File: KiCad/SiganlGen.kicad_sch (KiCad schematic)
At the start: 79 parts, among them J1 Barrel_Jack_MountingPin, J2 Conn_Coaxial, J3 Conn_01x08_Socket, Q1 BC557, Q2 BC547, SW1 RotaryEncoder_Switch, SW10 SW_Push_45deg, SW11 SW_Push_45deg, SW12 SW_Push_45deg, SW13 SW_Push_45deg, SW14 SW_Push_45deg, SW15 SW_Push_45deg, SW16 SW_Push_45deg, SW17 SW_Push_45deg, SW18 SW_Push, SW19 SW_Push, SW2 SW_Push_45deg, SW20 SW_Push, SW21 SW_Push, SW3 SW_Push_45deg, SW4 SW_Push_45deg, SW5 SW_Push_45deg, SW6 SW_Push_45deg, SW7 SW_Push_45deg, SW8 SW_Push_45deg, SW9 SW_Push_45deg, U1 RaspberryPi_Pico, U3 NE5532, U4 MC34063AP, U5 NE5532, U6 LM7910_TO220, U7 LM7810_TO220, U8 LM7805_TO220

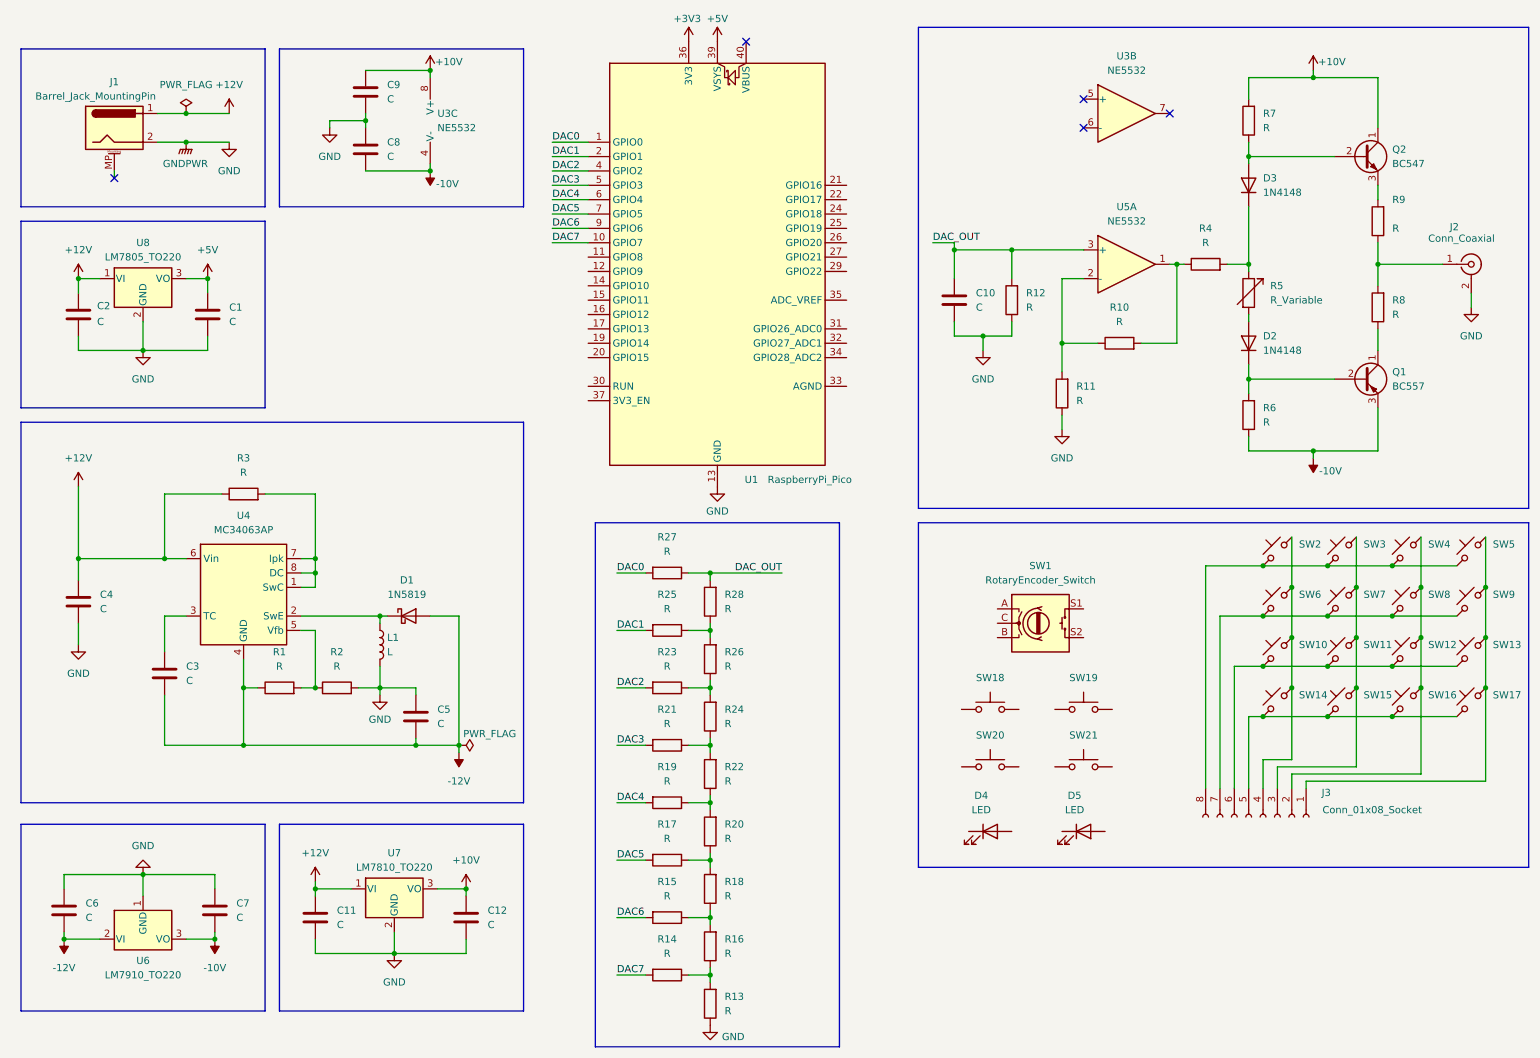
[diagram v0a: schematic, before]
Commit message: Partition schematic to different sheets
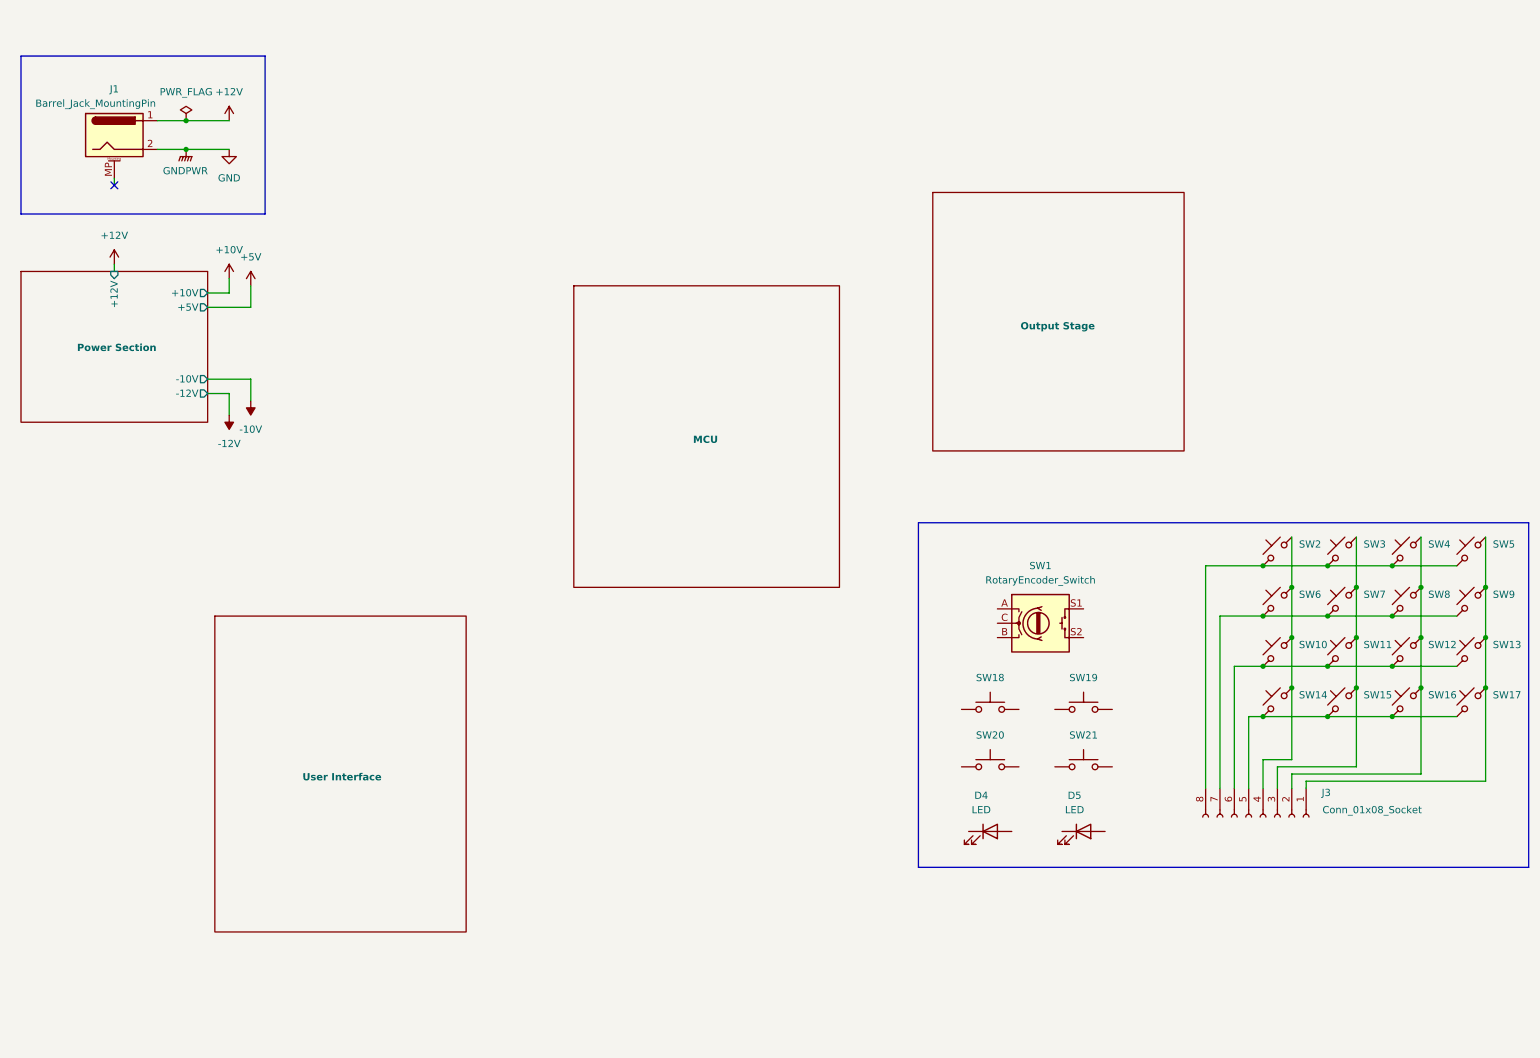
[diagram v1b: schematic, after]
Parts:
- removed C1, C10, C11, C12, C2, C3, C4, C5, C6, C7, C8, C9: C, symbol Device:C
- removed D1: 1N5819, Diode_THT:D_DO-41_SOD81_P10.16mm_Horizontal, symbol Diode:1N5819
- removed D2, D3: 1N4148, Diode_THT:D_DO-35_SOD27_P7.62mm_Horizontal, symbol Diode:1N4148
- removed J2: Conn_Coaxial, symbol Connector:Conn_Coaxial
- removed L1: L, symbol Device:L
- removed Q1: BC557, Package_TO_SOT_THT:TO-92_HandSolder, symbol Transistor_BJT:BC557
- removed Q2: BC547, Package_TO_SOT_THT:TO-92_HandSolder, symbol Transistor_BJT:BC547
- removed R1, R10, R11, R12, R13, R14, R15, R16, R17, R18, R19, R2, R20, R21, R22, R23, R24, R25, R26, R27, R28, R3, R4, R6, R7, R8, R9: R, symbol Device:R
- removed R5: R_Variable, symbol Device:R_Variable
- removed U1: RaspberryPi_Pico, Module_RaspberryPi_Pico:RaspberryPi_Pico_Common, symbol MCU_Module_RaspberryPi_Pico:RaspberryPi_Pico
- removed U3, U5: NE5532, Package_DIP:DIP-8_W7.62mm_Socket_LongPads, symbol Amplifier_Operational:NE5532
- removed U4: MC34063AP, Package_DIP:DIP-8_W7.62mm_Socket_LongPads, symbol Regulator_Switching:MC34063AP
- removed U6: LM7910_TO220, Package_TO_SOT_THT:TO-220-3_Vertical, symbol Regulator_Linear:LM7910_TO220
- removed U7: LM7810_TO220, Package_TO_SOT_THT:TO-220-3_Vertical, symbol Regulator_Linear:LM7810_TO220
- removed U8: LM7805_TO220, Package_TO_SOT_THT:TO-220-3_Vertical, symbol Regulator_Linear:LM7805_TO220
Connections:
- no-connect marks 5 -> 1
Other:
- added sheet MCU (MCU.kicad_sch)
- added sheet Output Stage (OutputStage.kicad_sch)
- added sheet Power Section (PowerSection.kicad_sch)
- added sheet User Interface (UserInterface.kicad_sch)
- moved on the sheet: J1

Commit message: Filled in schematic
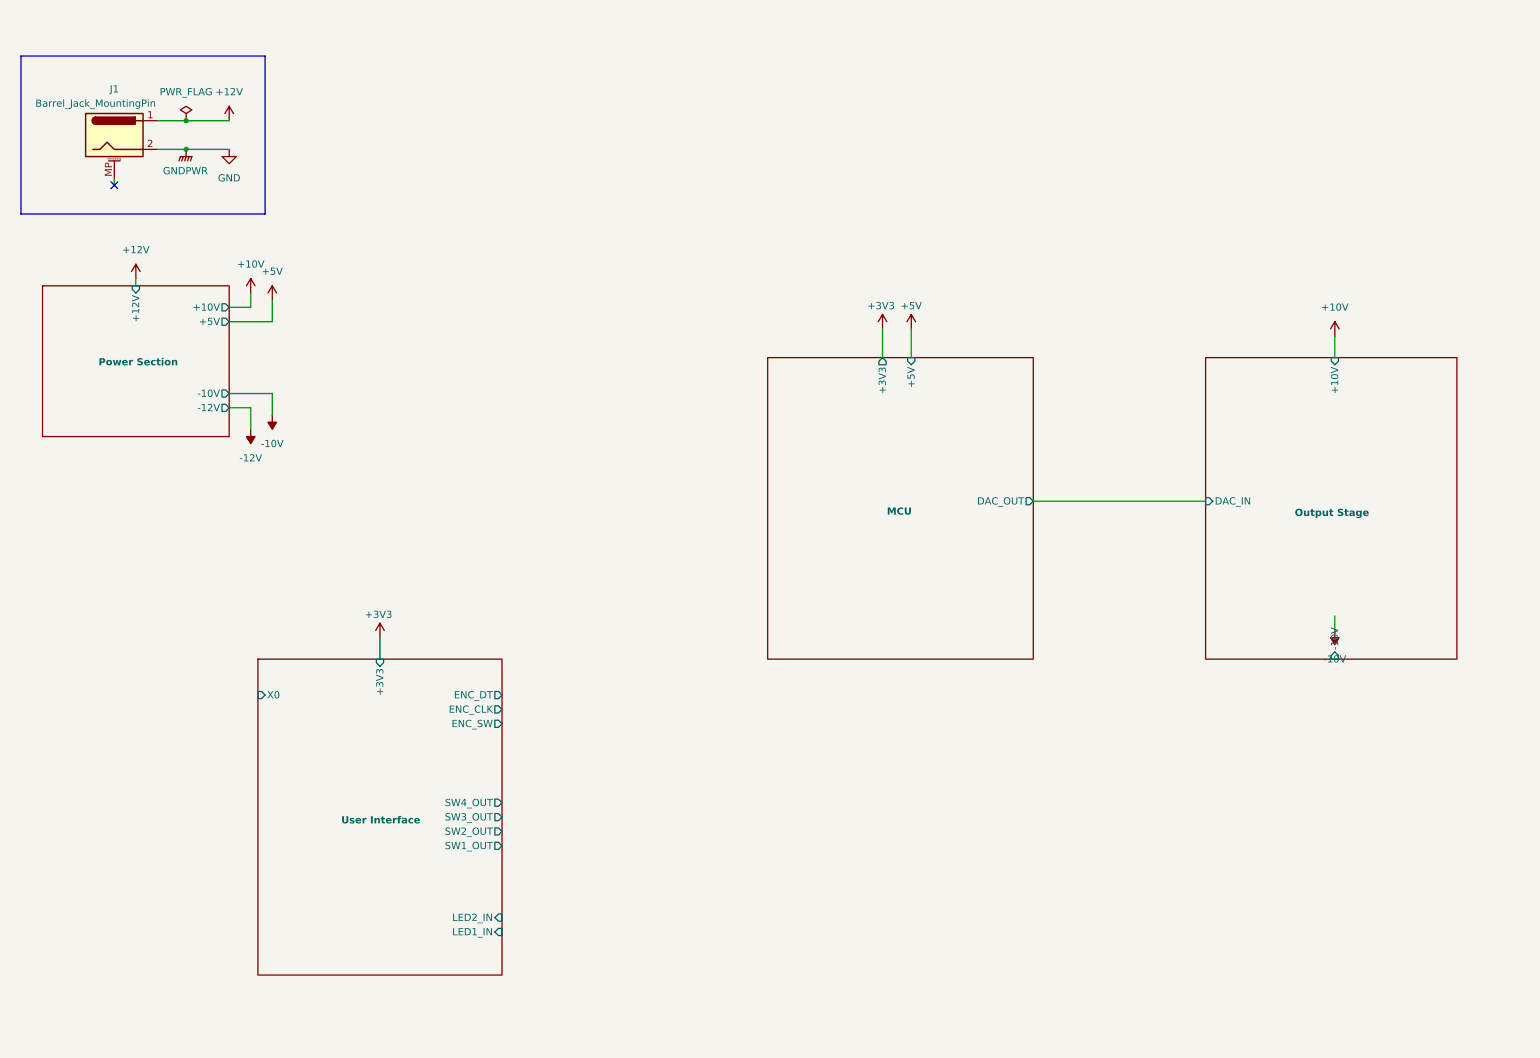
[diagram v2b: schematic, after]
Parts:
- removed D4, D5: LED, symbol Device:LED
- removed J3: Conn_01x08_Socket, symbol Connector:Conn_01x08_Socket
- removed SW1: RotaryEncoder_Switch, symbol Device:RotaryEncoder_Switch
- removed SW10, SW11, SW12, SW13, SW14, SW15, SW16, SW17, SW2, SW3, SW4, SW5, SW6, SW7, SW8, SW9: SW_Push_45deg, symbol Switch:SW_Push_45deg
- removed SW18, SW19, SW20, SW21: SW_Push, symbol Switch:SW_Push
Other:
- sheet MCU ports: added +3V3, +5V, DAC_OUT; removed none
- sheet Output Stage ports: added +10V, -10V, DAC_IN; removed none
- sheet User Interface ports: added +3V3, ENC_CLK, ENC_DT, ENC_SW, LED1_IN, LED2_IN, SW1_OUT, SW2_OUT, SW3_OUT, SW4_OUT, X0; removed none

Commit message: minor changes
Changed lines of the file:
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@@
 	(wire
 		(pts
-			(xy 195.58 99.06) (xy 226.06 99.06)
+			(xy 179.07 85.09) (xy 209.55 85.09)
 		)
 		(stroke
@@
 	(wire
 		(pts
-			(xy 173.99 68.58) (xy 173.99 73.66)
+			(xy 157.48 54.61) (xy 157.48 59.69)
 		)
 		(stroke
@@
 	(wire
 		(pts
-			(xy 248.92 119.38) (xy 248.92 121.92)
-		)
-		(stroke
-			(width 0)
-			(type default)
-		)
-	)
-	(wire
-		(pts
-			(xy 168.91 68.58) (xy 168.91 73.66)
+			(xy 232.41 105.41) (xy 232.41 107.95)
+		)
+		(stroke
+			(width 0)
+			(type default)
+		)
+	)
+	(wire
+		(pts
+			(xy 152.4 54.61) (xy 152.4 59.69)
 		)
 		(stroke
@@
 	(wire
 		(pts
-			(xy 248.92 69.85) (xy 248.92 73.66)
+			(xy 232.41 55.88) (xy 232.41 59.69)
 		)
 		(stroke
@@
 	(symbol
 		(lib_id "power:+3V3")
-		(at 168.91 68.58 0)
+		(at 152.4 54.61 0)
 		(unit 1)
 		(exclude_from_sim no)
@@
 		(dnp no)
 		(property "Reference" "#PWR011"
-			(at 168.91 72.39 0)
+			(at 152.4 58.42 0)
 			(effects
 				(font
@@
 		)
 		(property "Value" "+3V3"
-			(at 168.656 64.516 0)
+			(at 152.146 50.546 0)
 			(effects
 				(font
@@
 		)
 		(property "Footprint" ""
-			(at 168.91 68.58 0)
+			(at 152.4 54.61 0)
 			(effects
 				(font
@@
 		)
 		(property "Datasheet" ""
-			(at 168.91 68.58 0)
+			(at 152.4 54.61 0)
 			(effects
 				(font
@@
 		)
 		(property "Description" "Power symbol creates a global label with name \"+3V3\""
-			(at 168.91 68.58 0)
+			(at 152.4 54.61 0)
 			(effects
 				(font
@@
 	(symbol
 		(lib_id "power:+5V")
-		(at 173.99 68.58 0)
+		(at 157.48 54.61 0)
 		(unit 1)
 		(exclude_from_sim no)
@@
 		(dnp no)
 		(property "Reference" "#PWR016"
-			(at 173.99 72.39 0)
+			(at 157.48 58.42 0)
 			(effects
 				(font
@@
 		)
 		(property "Value" "+5V"
-			(at 173.99 64.516 0)
+			(at 157.48 50.546 0)
 			(effects
 				(font
@@
 		)
 		(property "Footprint" ""
-			(at 173.99 68.58 0)
+			(at 157.48 54.61 0)
 			(effects
 				(font
@@
 		)
 		(property "Datasheet" ""
-			(at 173.99 68.58 0)
+			(at 157.48 54.61 0)
 			(effects
 				(font
@@
 		)
 		(property "Description" "Power symbol creates a global label with name \"+5V\""
-			(at 173.99 68.58 0)
+			(at 157.48 54.61 0)
 			(effects
 				(font
@@
 	(symbol
 		(lib_id "power:+10V")
-		(at 248.92 69.85 0)
+		(at 232.41 55.88 0)
 		(unit 1)
 		(exclude_from_sim no)
@@
 		(fields_autoplaced yes)
 		(property "Reference" "#PWR021"
-			(at 248.92 73.66 0)
+			(at 232.41 59.69 0)
 			(effects
 				(font
@@
 		)
 		(property "Value" "+10V"
-			(at 248.92 64.77 0)
+			(at 232.41 50.8 0)
 			(effects
 				(font
@@
 		)
 		(property "Footprint" ""
-			(at 248.92 69.85 0)
+			(at 232.41 55.88 0)
 			(effects
 				(font
@@
 		)
 		(property "Datasheet" ""
-			(at 248.92 69.85 0)
+			(at 232.41 55.88 0)
 			(effects
 				(font
@@
 		)
 		(property "Description" "Power symbol creates a global label with name \"+10V\""
-			(at 248.92 69.85 0)
+			(at 232.41 55.88 0)
 			(effects
 				(font
@@
 	(symbol
 		(lib_id "power:-10V")
-		(at 248.92 121.92 180)
+		(at 232.41 107.95 180)
 		(unit 1)
 		(exclude_from_sim no)
@@
 		(fields_autoplaced yes)
 		(property "Reference" "#PWR018"
-			(at 248.92 118.11 0)
+			(at 232.41 104.14 0)
 			(effects
 				(font
@@
 		)
 		(property "Value" "-10V"
-			(at 248.92 127 0)
+			(at 232.41 113.03 0)
 			(effects
 				(font
@@
 		)
 		(property "Footprint" ""
-			(at 248.92 121.92 0)
+			(at 232.41 107.95 0)
 			(effects
 				(font
@@
 		)
 		(property "Datasheet" ""
-			(at 248.92 121.92 0)
+			(at 232.41 107.95 0)
 			(effects
 				(font
@@
 		)
 		(property "Description" "Power symbol creates a global label with name \"-10V\""
-			(at 248.92 121.92 0)
+			(at 232.41 107.95 0)
 			(effects
 				(font
@@
 	)
 	(sheet
-		(at 148.59 73.66)
+		(at 132.08 59.69)
 		(size 46.99 53.34)
 		(stroke
@@
 		)
 		(property "Sheetname" "MCU"
-			(at 169.672 101.6 0)
+			(at 153.162 87.63 0)
 			(effects
 				(font
@@
 		)
 		(property "Sheetfile" "MCU.kicad_sch"
-			(at 148.59 127.5846 0)
+			(at 132.08 113.6146 0)
 			(effects
 				(font
@@
 		)
 		(pin "+3V3" output
-			(at 168.91 73.66 90)
+			(at 152.4 59.69 90)
 			(effects
 				(font
@@
 		)
 		(pin "+5V" input
-			(at 173.99 73.66 90)
+			(at 157.48 59.69 90)
 			(effects
 				(font
@@
 		)
 		(pin "DAC_OUT" output
-			(at 195.58 99.06 0)
+			(at 179.07 85.09 0)
 			(effects
 				(font
@@
 	)
 	(sheet
-		(at 226.06 73.66)
+		(at 209.55 59.69)
 		(size 44.45 53.34)
 		(stroke
@@
 		)
 		(property "Sheetname" "Output Stage"
-			(at 248.412 101.092 0)
+			(at 231.902 87.122 0)
 			(effects
 				(font
@@
 		)
 		(property "Sheetfile" "OutputStage.kicad_sch"
-			(at 226.06 119.9646 0)
+			(at 209.55 105.9946 0)
 			(effects
 				(font
@@
 		)
 		(pin "DAC_IN" input
-			(at 226.06 99.06 180)
+			(at 209.55 85.09 180)
 			(effects
 				(font
@@
 		)
 		(pin "-10V" input
-			(at 248.92 127 270)
+			(at 232.41 113.03 270)
 			(effects
 				(font
@@
 		)
 		(pin "+10V" input
-			(at 248.92 73.66 90)
-			(effects
-				(font
+			(at 232.41 59.69 90)
+			(effects
+				(font
